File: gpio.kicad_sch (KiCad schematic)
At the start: 5 parts, among them J1 CONN_02X20, J2 CONN_02X20, U1 LFE5U-85F-6BG381C

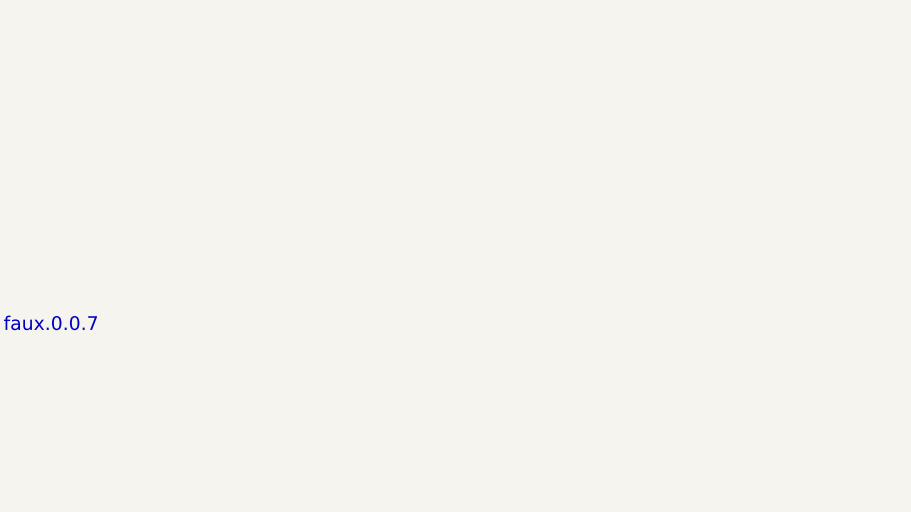
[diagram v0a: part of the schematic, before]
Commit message: broken: shrink board, re-orient parts. mid-progress, before 4-6 layer
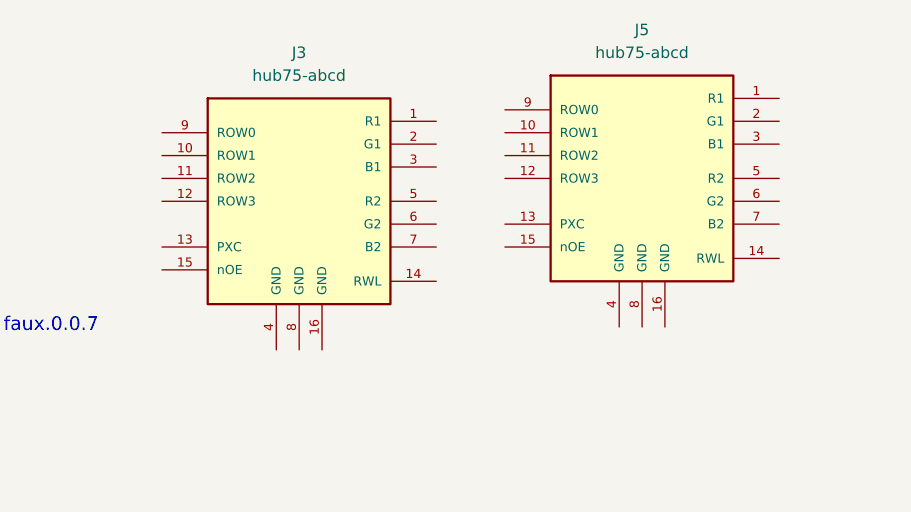
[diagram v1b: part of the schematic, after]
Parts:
- added J3, J5: hub75-abcd, Socket_Strips:SAMTEC-HTST-108-01-X-DV, symbol samtec:hub75-abcd

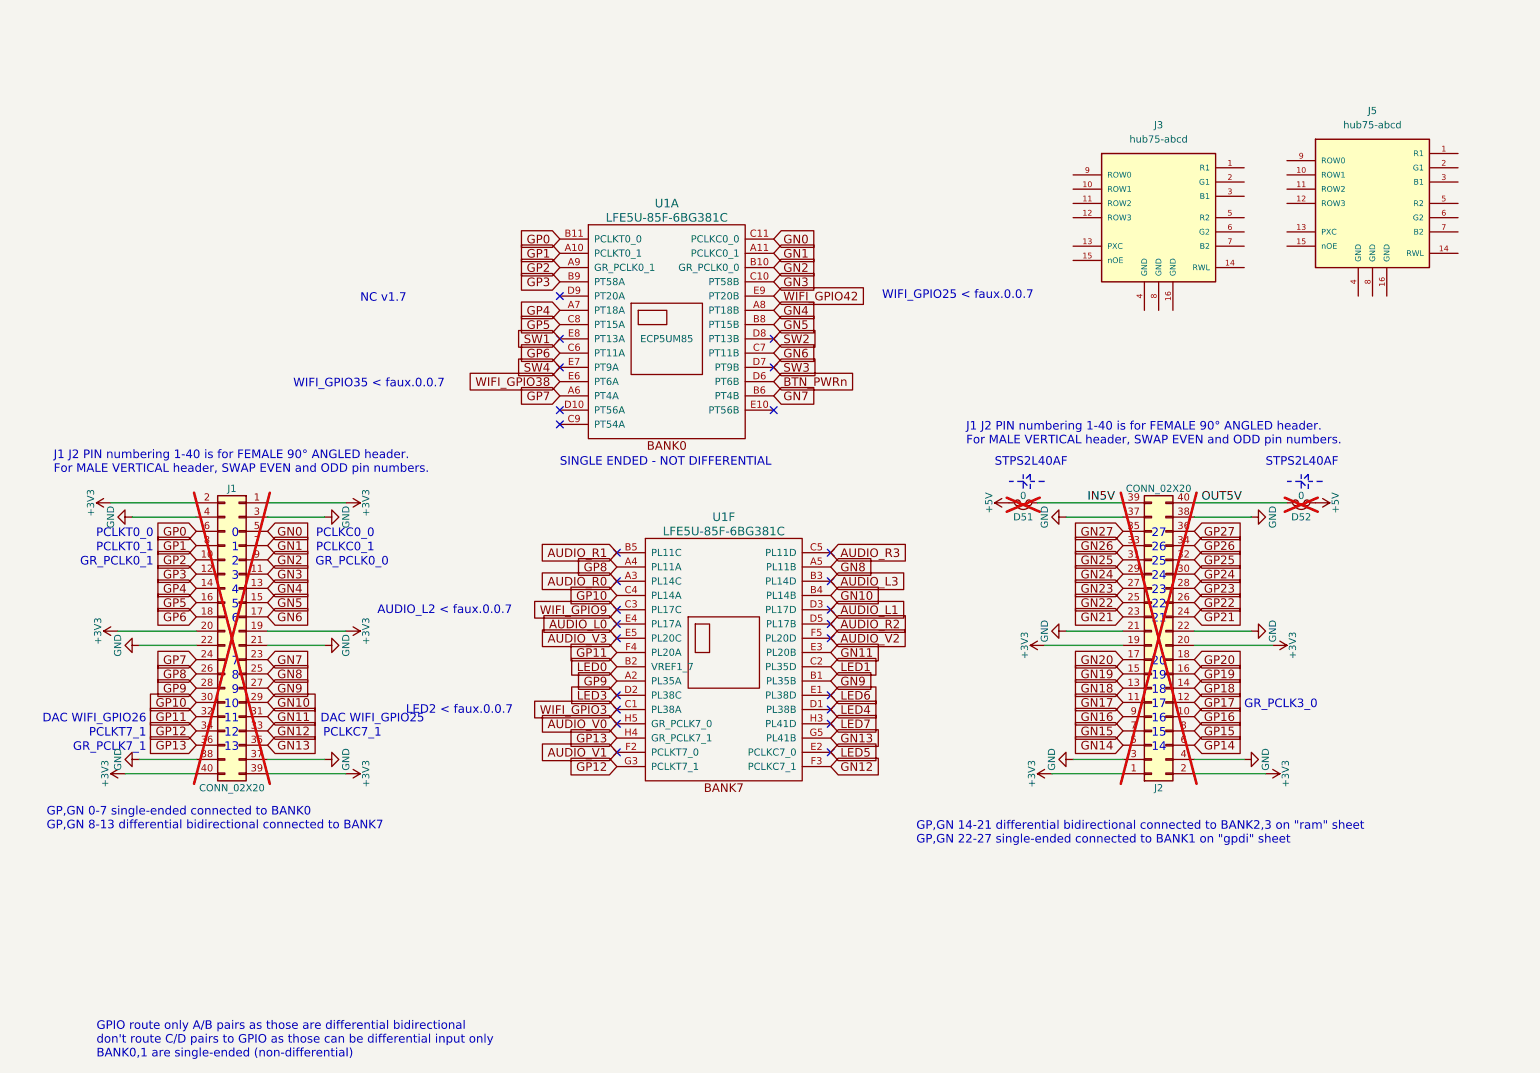
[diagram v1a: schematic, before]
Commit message: reassign j1 signals
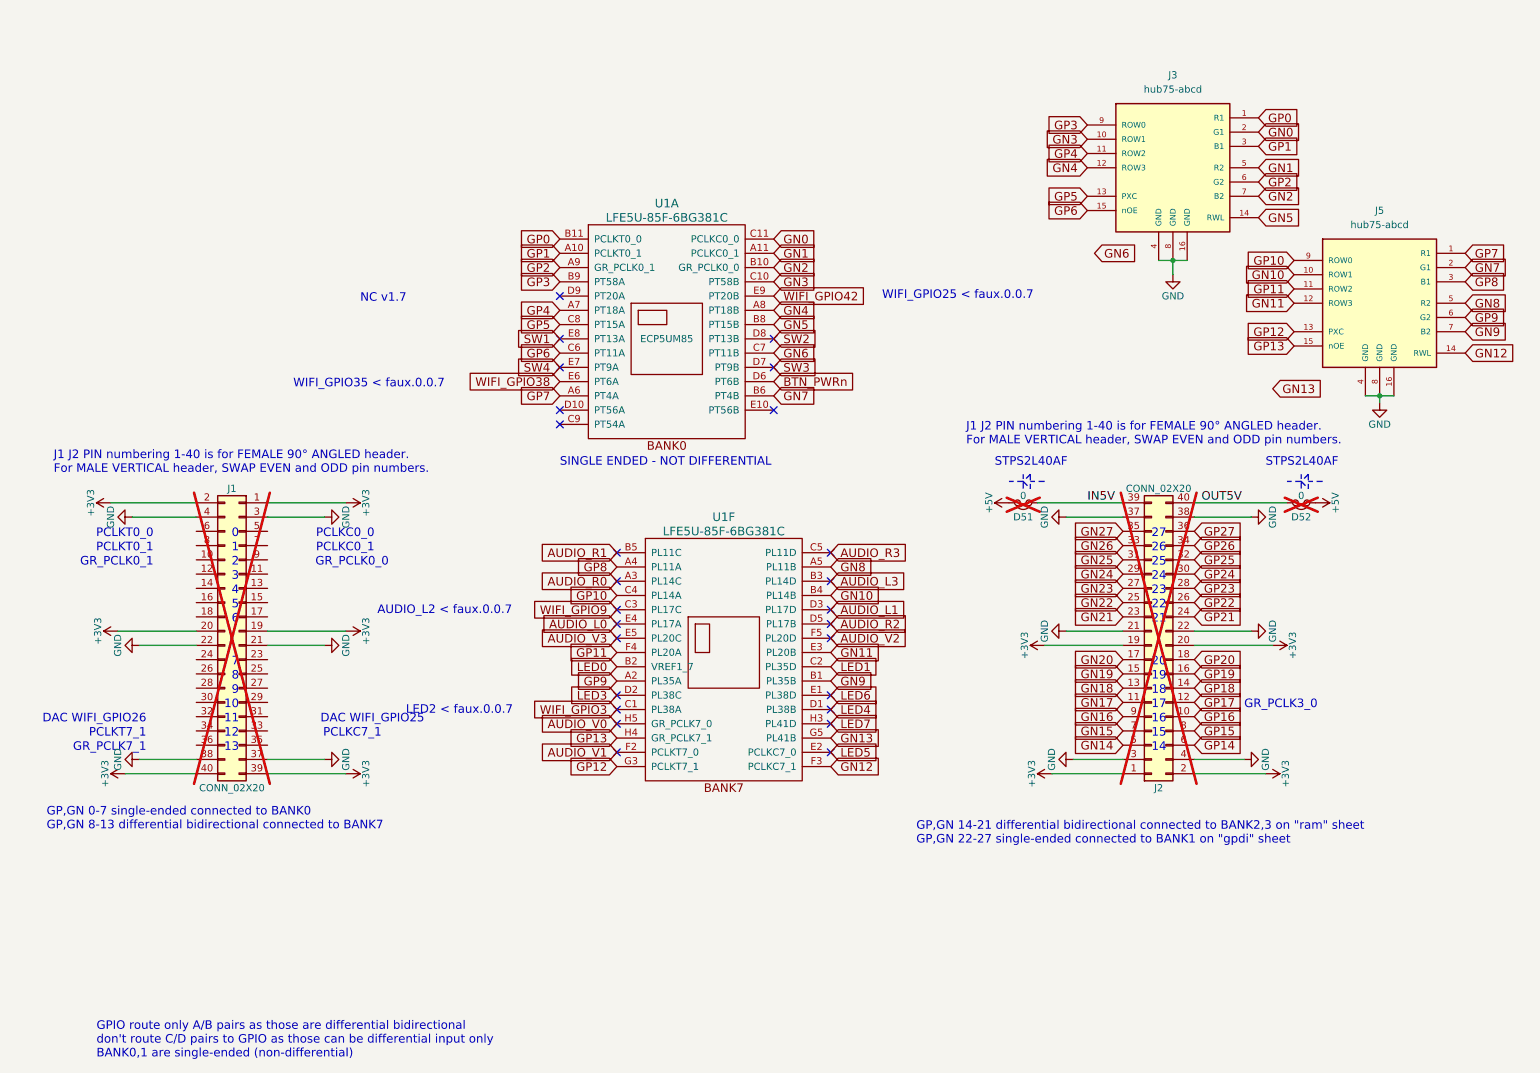
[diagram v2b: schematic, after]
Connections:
- net GN0: now also J3.2 (G1); no longer J1.5 (Pin_5)
- net GN1: now also J3.5 (R2); no longer J1.7 (Pin_7)
- net GN10: now also J5.10 (ROW1); no longer J1.29 (Pin_29)
- net GN11: now also J5.12 (ROW3); no longer J1.31 (Pin_31)
- net GN12: now also J5.14 (RWL); no longer J1.33 (Pin_33)
- net GN13: no longer J1.35 (Pin_35)
- net GN2: now also J3.7 (B2); no longer J1.9 (Pin_9)
- net GN3: now also J3.10 (ROW1); no longer J1.11 (Pin_11)
- net GN4: now also J3.12 (ROW3); no longer J1.13 (Pin_13)
- net GN5: now also J3.14 (RWL); no longer J1.15 (Pin_15)
- net GN6: no longer J1.17 (Pin_17)
- net GN7: now also J5.2 (G1); no longer J1.23 (Pin_23)
- net GN8: now also J5.5 (R2); no longer J1.25 (Pin_25)
- net GN9: now also J5.7 (B2); no longer J1.27 (Pin_27)
- net GND: now also J3.16 (GND), J3.4 (GND), J3.8 (GND), J5.16 (GND), J5.4 (GND), J5.8 (GND)
- net GP0: now also J3.1 (R1); no longer J1.6 (Pin_6)
- net GP1: now also J3.3 (B1); no longer J1.8 (Pin_8)
- net GP10: now also J5.9 (ROW0); no longer J1.30 (Pin_30)
- net GP11: now also J5.11 (ROW2); no longer J1.32 (Pin_32)
- net GP12: now also J5.13 (PXC); no longer J1.34 (Pin_34)
- net GP13: now also J5.15 (nOE); no longer J1.36 (Pin_36)
- net GP2: now also J3.6 (G2); no longer J1.10 (Pin_10)
- net GP3: now also J3.9 (ROW0); no longer J1.12 (Pin_12)
- net GP4: now also J3.11 (ROW2); no longer J1.14 (Pin_14)
- net GP5: now also J3.13 (PXC); no longer J1.16 (Pin_16)
- net GP6: now also J3.15 (nOE); no longer J1.18 (Pin_18)
- net GP7: now also J5.1 (R1); no longer J1.24 (Pin_24)
- net GP8: now also J5.3 (B1); no longer J1.26 (Pin_26)
- net GP9: now also J5.6 (G2); no longer J1.28 (Pin_28)
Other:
- moved on the sheet: J3, J5

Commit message: in progress, placement happend -- working on wiring
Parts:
- J3, J5: Digikey (none) -> SAM14030CT-ND; MPN (none) -> 200-HTST10801LDVP

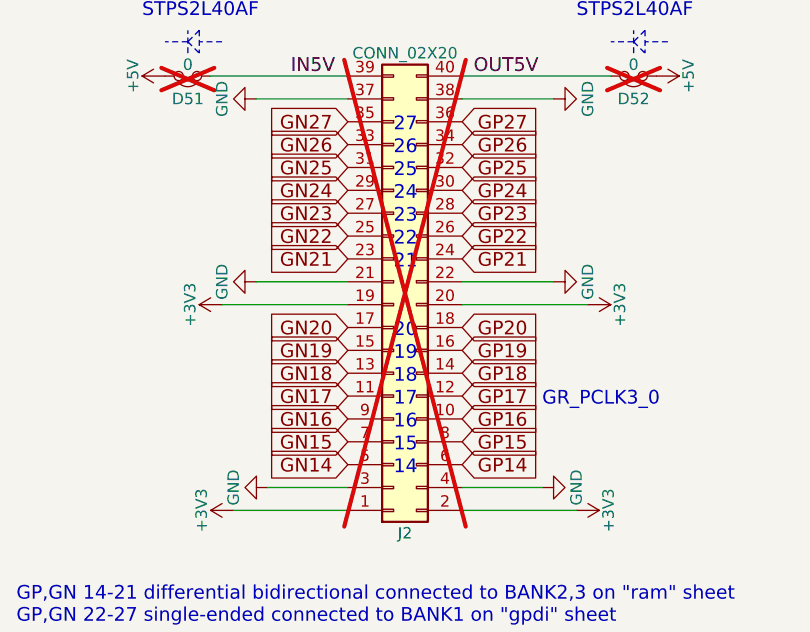
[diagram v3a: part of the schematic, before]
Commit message: done with routing
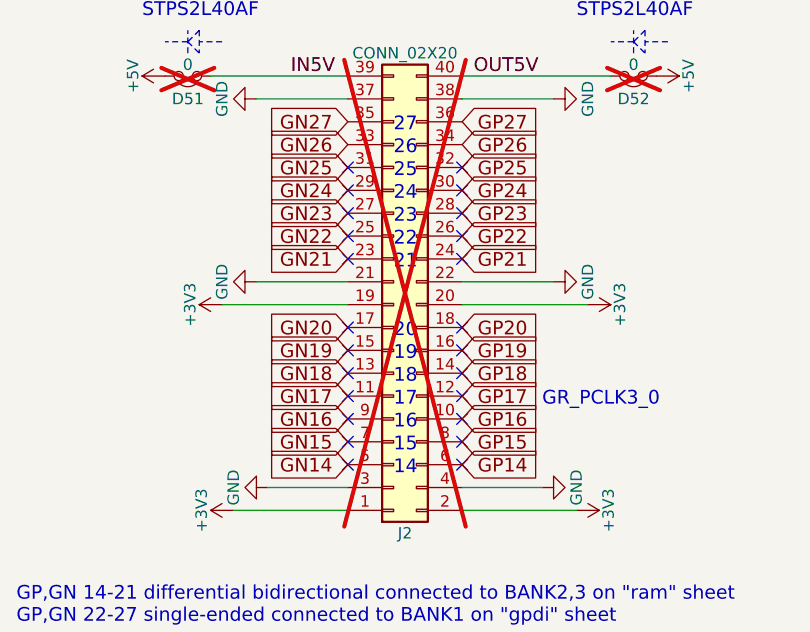
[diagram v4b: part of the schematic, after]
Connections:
- no-connect marks 26 -> 50
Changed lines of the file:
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@@
 	)
 	(no_connect
+		(at 207.01 113.03)
+	)
+	(no_connect
 		(at 154.94 129.54)
 	)
 	(no_connect
+		(at 207.01 120.65)
+	)
+	(no_connect
 		(at 116.84 101.6)
 	)
@@
 	)
 	(no_connect
+		(at 207.01 133.35)
+	)
+	(no_connect
 		(at 116.84 111.76)
 	)
@@
 	)
 	(no_connect
+		(at 219.71 105.41)
+	)
+	(no_connect
+		(at 219.71 123.19)
+	)
+	(no_connect
+		(at 219.71 128.27)
+	)
+	(no_connect
+		(at 219.71 102.87)
+	)
+	(no_connect
+		(at 219.71 133.35)
+	)
+	(no_connect
+		(at 219.71 107.95)
+	)
+	(no_connect
 		(at 106.68 55.88)
 	)
 	(no_connect
+		(at 207.01 128.27)
+	)
+	(no_connect
 		(at 116.84 137.16)
 	)
@@
 	)
 	(no_connect
+		(at 219.71 110.49)
+	)
+	(no_connect
 		(at 116.84 116.84)
 	)
@@
 	)
 	(no_connect
+		(at 219.71 125.73)
+	)
+	(no_connect
 		(at 106.68 68.58)
 	)
@@
 	)
 	(no_connect
+		(at 207.01 135.89)
+	)
+	(no_connect
 		(at 154.94 132.08)
 	)
@@
 	)
 	(no_connect
+		(at 219.71 120.65)
+	)
+	(no_connect
+		(at 207.01 107.95)
+	)
+	(no_connect
+		(at 207.01 130.81)
+	)
+	(no_connect
+		(at 219.71 113.03)
+	)
+	(no_connect
+		(at 207.01 125.73)
+	)
+	(no_connect
 		(at 116.84 127)
 	)
@@
 	)
 	(no_connect
+		(at 219.71 135.89)
+	)
+	(no_connect
 		(at 144.78 68.58)
 	)
@@
 	)
 	(no_connect
+		(at 207.01 123.19)
+	)
+	(no_connect
+		(at 219.71 130.81)
+	)
+	(no_connect
 		(at 154.94 106.68)
 	)
 	(no_connect
+		(at 207.01 102.87)
+	)
+	(no_connect
 		(at 144.78 76.2)
 	)
@@
 	)
 	(no_connect
+		(at 207.01 105.41)
+	)
+	(no_connect
+		(at 207.01 110.49)
+	)
+	(no_connect
 		(at 106.68 76.2)
 	)
@@
 		(exclude_from_sim no)
 		(in_bom no)
-		(on_board yes)
+		(on_board no)
 		(in_pos_files no)
 		(dnp yes)
@@
 		(exclude_from_sim no)
 		(in_bom no)
-		(on_board yes)
+		(on_board no)
 		(in_pos_files no)
 		(dnp yes)

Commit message: switch to usb-c. upgrade to v1.0.4
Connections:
- no-connect marks 50 -> 82
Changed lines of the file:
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@@
+	)
+	(no_connect
+		(at 41.91 110.49)
 	)
 	(no_connect
@@
 	)
 	(no_connect
+		(at 41.91 100.33)
+	)
+	(no_connect
+		(at 41.91 135.89)
+	)
+	(no_connect
+		(at 201.93 48.26)
+	)
+	(no_connect
 		(at 207.01 120.65)
 	)
@@
 	)
 	(no_connect
+		(at 144.78 66.04)
+	)
+	(no_connect
+		(at 54.61 123.19)
+	)
+	(no_connect
+		(at 54.61 135.89)
+	)
+	(no_connect
 		(at 154.94 111.76)
 	)
 	(no_connect
+		(at 54.61 107.95)
+	)
+	(no_connect
 		(at 207.01 133.35)
 	)
 	(no_connect
+		(at 41.91 102.87)
+	)
+	(no_connect
+		(at 41.91 120.65)
+	)
+	(no_connect
 		(at 116.84 111.76)
 	)
 	(no_connect
+		(at 41.91 133.35)
+	)
+	(no_connect
+		(at 54.61 133.35)
+	)
+	(no_connect
 		(at 116.84 132.08)
 	)
@@
 	)
 	(no_connect
+		(at 54.61 128.27)
+	)
+	(no_connect
+		(at 41.91 97.79)
+	)
+	(no_connect
 		(at 219.71 123.19)
 	)
 	(no_connect
+		(at 154.94 134.62)
+	)
+	(no_connect
 		(at 219.71 128.27)
 	)
@@
 	)
 	(no_connect
+		(at 41.91 105.41)
+	)
+	(no_connect
 		(at 106.68 55.88)
 	)
@@
 	)
 	(no_connect
+		(at 54.61 125.73)
+	)
+	(no_connect
 		(at 154.94 116.84)
 	)
@@
 	)
 	(no_connect
+		(at 54.61 105.41)
+	)
+	(no_connect
 		(at 144.78 63.5)
 	)
 	(no_connect
+		(at 41.91 107.95)
+	)
+	(no_connect
+		(at 41.91 130.81)
+	)
+	(no_connect
 		(at 219.71 110.49)
 	)
@@
 	)
 	(no_connect
+		(at 54.61 110.49)
+	)
+	(no_connect
+		(at 233.68 72.39)
+	)
+	(no_connect
 		(at 106.68 63.5)
 	)
@@
 	)
 	(no_connect
+		(at 54.61 100.33)
+	)
+	(no_connect
 		(at 106.68 68.58)
 	)
@@
 	)
 	(no_connect
+		(at 54.61 97.79)
+	)
+	(no_connect
 		(at 207.01 135.89)
 	)
 	(no_connect
+		(at 54.61 120.65)
+	)
+	(no_connect
 		(at 154.94 132.08)
 	)
 	(no_connect
+		(at 41.91 123.19)
+	)
+	(no_connect
 		(at 116.84 114.3)
 	)
 	(no_connect
+		(at 41.91 128.27)
+	)
+	(no_connect
 		(at 106.68 78.74)
 	)
 	(no_connect
+		(at 54.61 102.87)
+	)
+	(no_connect
 		(at 219.71 120.65)
 	)
@@
 	)
 	(no_connect
+		(at 54.61 113.03)
+	)
+	(no_connect
 		(at 219.71 113.03)
 	)
 	(no_connect
+		(at 54.61 130.81)
+	)
+	(no_connect
 		(at 207.01 125.73)
 	)
@@
 	)
 	(no_connect
+		(at 41.91 113.03)
+	)
+	(no_connect
 		(at 207.01 105.41)
 	)
@@
 		(at 106.68 76.2)
 	)
+	(no_connect
+		(at 41.91 125.73)
+	)
 	(wire

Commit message: make MPN reflect mouser part numbers
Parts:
- U1: MPN LFE5U-85F-6BG381C -> 842-LFE5U85F6BG381C
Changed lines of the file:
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@@
 			)
 		)
-		(property "MPN" "LFE5U-85F-6BG381C"
+		(property "MPN" "842-LFE5U85F6BG381C"
 			(at 125.73 63.5 0)
 			(hide yes)
@@
 			)
 		)
-		(property "MPN" "LFE5U-85F-6BG381C"
+		(property "MPN" "842-LFE5U85F6BG381C"
 			(at 135.89 119.38 0)
 			(hide yes)

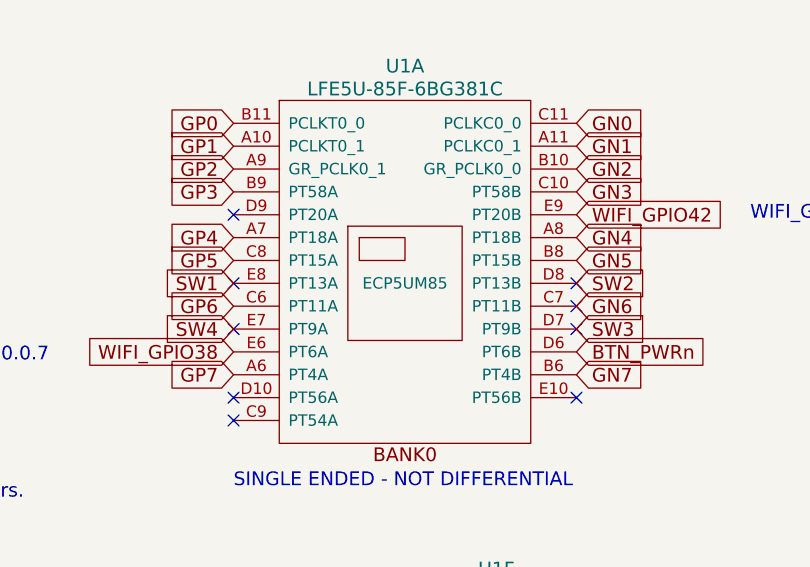
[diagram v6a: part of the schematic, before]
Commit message: update footprints to include additional border. add i2c resistors
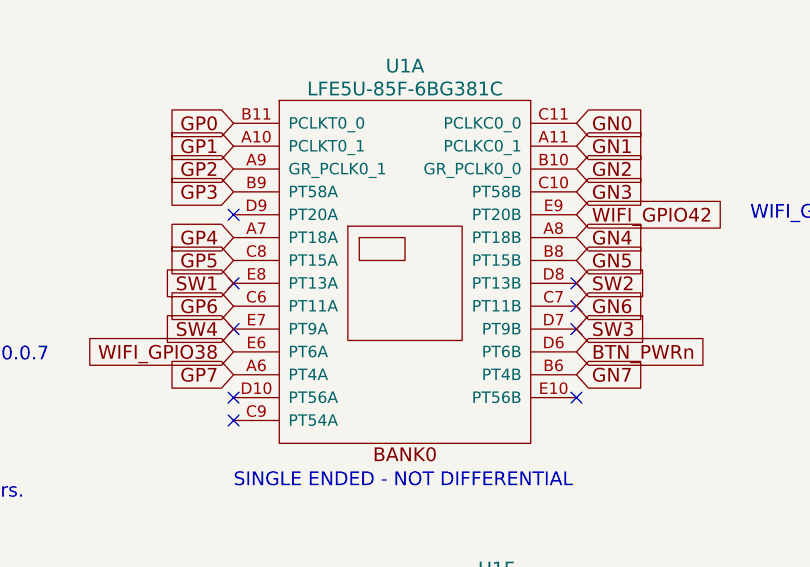
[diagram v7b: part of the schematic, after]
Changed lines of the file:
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@@
 			)
 		)
-		(property "Datasheet" "http://www.latticesemi.com/~/media/LatticeSemi/Documents/DataSheets/ECP5/FPGA-DS-02012.pdf"
+		(property "Datasheet" "https://www.mouser.com/datasheet/3/248/1/FPGA_DS_02012_3_4_ECP5_ECP5G_Family_Data_Sheet.pdf"
 			(at 99.06 39.37 0)
 			(hide yes)
@@
 			)
 		)
-		(property "Description" "ECP5UM85"
+		(property "Description" ""
 			(at 125.73 63.5 0)
 			(show_name no)
@@
 			)
 		)
-		(property "Datasheet" "http://www.latticesemi.com/~/media/LatticeSemi/Documents/DataSheets/ECP5/FPGA-DS-02012.pdf"
+		(property "Datasheet" "https://www.mouser.com/datasheet/3/248/1/FPGA_DS_02012_3_4_ECP5_ECP5G_Family_Data_Sheet.pdf"
 			(at 109.22 95.25 0)
 			(hide yes)
